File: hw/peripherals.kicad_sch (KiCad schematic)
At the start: 22 parts, among them Q2 N-Channel, SW1 SW_DPST, U10 MB85RC256VPNF-G-JNERE1, U11 DS3231M, U9 PCA9536D

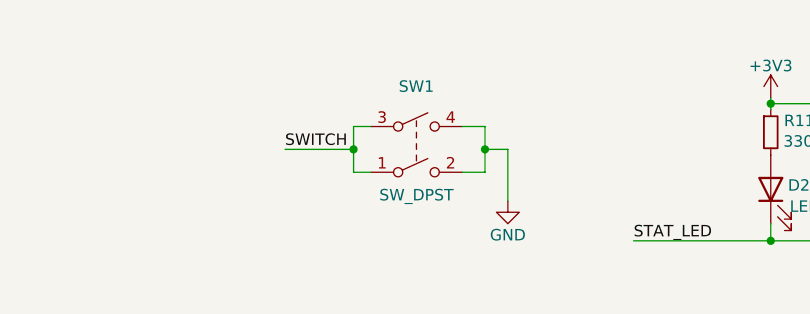
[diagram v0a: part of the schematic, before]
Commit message: hw: use CR2032 footprint & larger testpoints
Signed-off-by: Mahyar Koshkouei <mk@deltabeard.com>
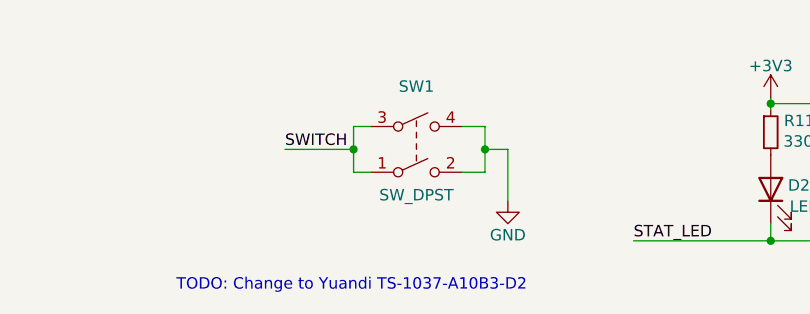
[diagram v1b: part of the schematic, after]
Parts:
- BT1: footprint Battery:BatteryHolder_Keystone_3000_1x12mm -> Project_Specific:MY-2032-11; LCSC C964818 -> C964835; MFr MY-1220-03 -> MY-2032-11
- TP40, TP41, TP42, TP43, TP44, TP45: footprint Project_Specific:TestPoint_Pad_D0.5mm -> TestPoint:TestPoint_Pad_D1.0mm
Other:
- note added: "TODO: Change to Yuandi TS-1037-A10B3-D2"
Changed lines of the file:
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@@
     (stroke (width 0) (type solid) (color 0 0 0 0))
+  )
+  (text "TODO: Change to Yuandi TS-1037-A10B3-D2" (at 72.39 165.1 0)
+    (effects (font (size 1.27 1.27)) (justify left bottom))
   )
   (label "SWITCH" (at 84.455 149.225 0)
@@
       (effects (font (size 1.27 1.27)) hide)
     )
-    (property "Footprint" "Project_Specific:TestPoint_Pad_D0.5mm" (id 2) (at 52.705 118.11 0)
+    (property "Footprint" "TestPoint:TestPoint_Pad_D1.0mm" (id 2) (at 52.705 118.11 0)
       (effects (font (size 1.27 1.27)) hide)
     )
@@
       (effects (font (size 1.27 1.27)) hide)
     )
-    (property "Footprint" "Project_Specific:TestPoint_Pad_D0.5mm" (id 2) (at 52.7398 120.65 0)
+    (property "Footprint" "TestPoint:TestPoint_Pad_D1.0mm" (id 2) (at 52.7398 120.65 0)
       (effects (font (size 1.27 1.27)) hide)
     )
@@
       (effects (font (size 1.27 1.27)) hide)
     )
-    (property "Footprint" "Project_Specific:TestPoint_Pad_D0.5mm" (id 2) (at 118.11 120.65 0)
+    (property "Footprint" "TestPoint:TestPoint_Pad_D1.0mm" (id 2) (at 118.11 120.65 0)
       (effects (font (size 1.27 1.27)) hide)
     )
@@
       (effects (font (size 1.27 1.27)) hide)
     )
-    (property "Footprint" "Project_Specific:TestPoint_Pad_D0.5mm" (id 2) (at 119.3501 115.57 0)
+    (property "Footprint" "TestPoint:TestPoint_Pad_D1.0mm" (id 2) (at 119.3501 115.57 0)
       (effects (font (size 1.27 1.27)) hide)
     )
@@
       (effects (font (size 1.27 1.27)) hide)
     )
-    (property "Footprint" "Project_Specific:TestPoint_Pad_D0.5mm" (id 2) (at 119.3501 118.11 0)
+    (property "Footprint" "TestPoint:TestPoint_Pad_D1.0mm" (id 2) (at 119.3501 118.11 0)
       (effects (font (size 1.27 1.27)) hide)
     )
@@
       (effects (font (size 1.27 1.27)) hide)
     )
-    (property "Footprint" "Project_Specific:TestPoint_Pad_D0.5mm" (id 2) (at 119.38 113.03 0)
+    (property "Footprint" "TestPoint:TestPoint_Pad_D1.0mm" (id 2) (at 119.38 113.03 0)
       (effects (font (size 1.27 1.27)) hide)
     )
@@
       (effects (font (size 1.27 1.27)) (justify left))
     )
-    (property "Footprint" "Battery:BatteryHolder_Keystone_3000_1x12mm" (id 2) (at 84.455 53.721 90)
+    (property "Footprint" "Project_Specific:MY-2032-11" (id 2) (at 84.455 53.721 90)
       (effects (font (size 1.27 1.27)) hide)
     )
@@
       (effects (font (size 1.27 1.27)) hide)
     )
-    (property "LCSC" "C964818" (id 4) (at 84.455 55.245 0)
-      (effects (font (size 1.27 1.27)) hide)
-    )
-    (property "MFr" "MY-1220-03" (id 5) (at 84.455 55.245 0)
+    (property "LCSC" "C964835" (id 4) (at 84.455 55.245 0)
+      (effects (font (size 1.27 1.27)) hide)
+    )
+    (property "MFr" "MY-2032-11" (id 5) (at 84.455 55.245 0)
       (effects (font (size 1.27 1.27)) hide)
     )
@@
       (effects (font (size 1.27 1.27)) hide)
     )
-    (property "Description" "CR1220 Battery holder" (id 8) (at 84.455 55.245 0)
-      (effects (font (size 1.27 1.27)) hide)
-    )
+    (property "Description" "CR2032 Battery holder" (id 8) (at 84.455 55.245 0)
+      (effects (font (size 1.27 1.27)) hide)
+    )

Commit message: all: Add open source license
Signed-off-by: Mahyar Koshkouei <mk@deltabeard.com>
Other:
- company: Mahyar Koshkouei -> Copyright (c) 2021 Mahyar Koshkouei
- title: RP2040 Game Boy Cart -> DBGC: RP2040 Game Boy Cart
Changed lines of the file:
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@@
   (paper "A4")
   (title_block
-    (title "RP2040 Game Boy Cart")
+    (title "DBGC: RP2040 Game Boy Cart")
     (date "2021-09-29")
     (rev "0.3a")
-    (company "Mahyar Koshkouei")
-    (comment 1 "All Rights Reserved")
+    (company "Copyright (c) 2021 Mahyar Koshkouei")
+    (comment 1 "CC BY-SA 4.0")
     (comment 2 "Compatible with DMG, MGB, & CGB. Collectively referred to as \"GB\" here.")
   )
